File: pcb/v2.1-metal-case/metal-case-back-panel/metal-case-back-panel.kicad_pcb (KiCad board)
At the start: 2 copper layers, 50 x 20 mm, 6 parts

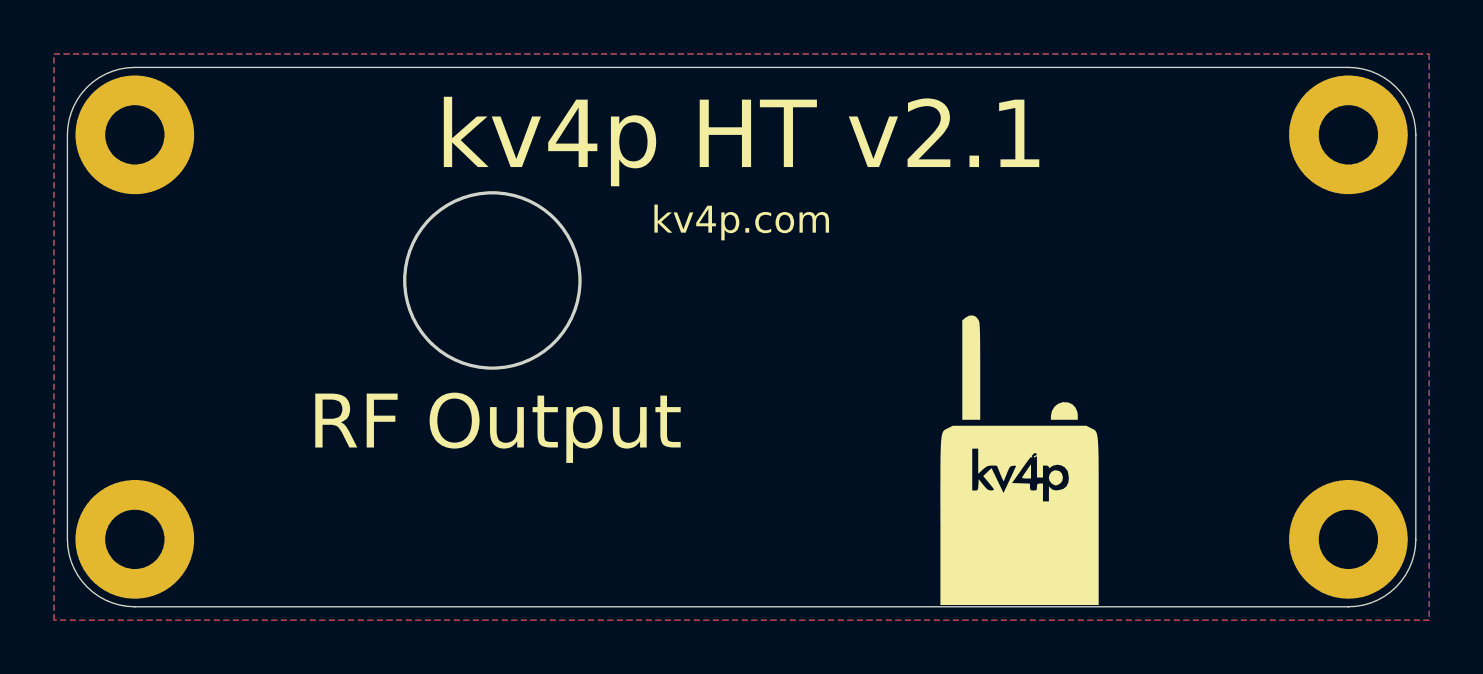
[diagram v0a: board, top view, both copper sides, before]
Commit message: v2.1b as ordered 2025-04-17. VHF and UHF #22. SAO headers. PTT buttons. User LED.
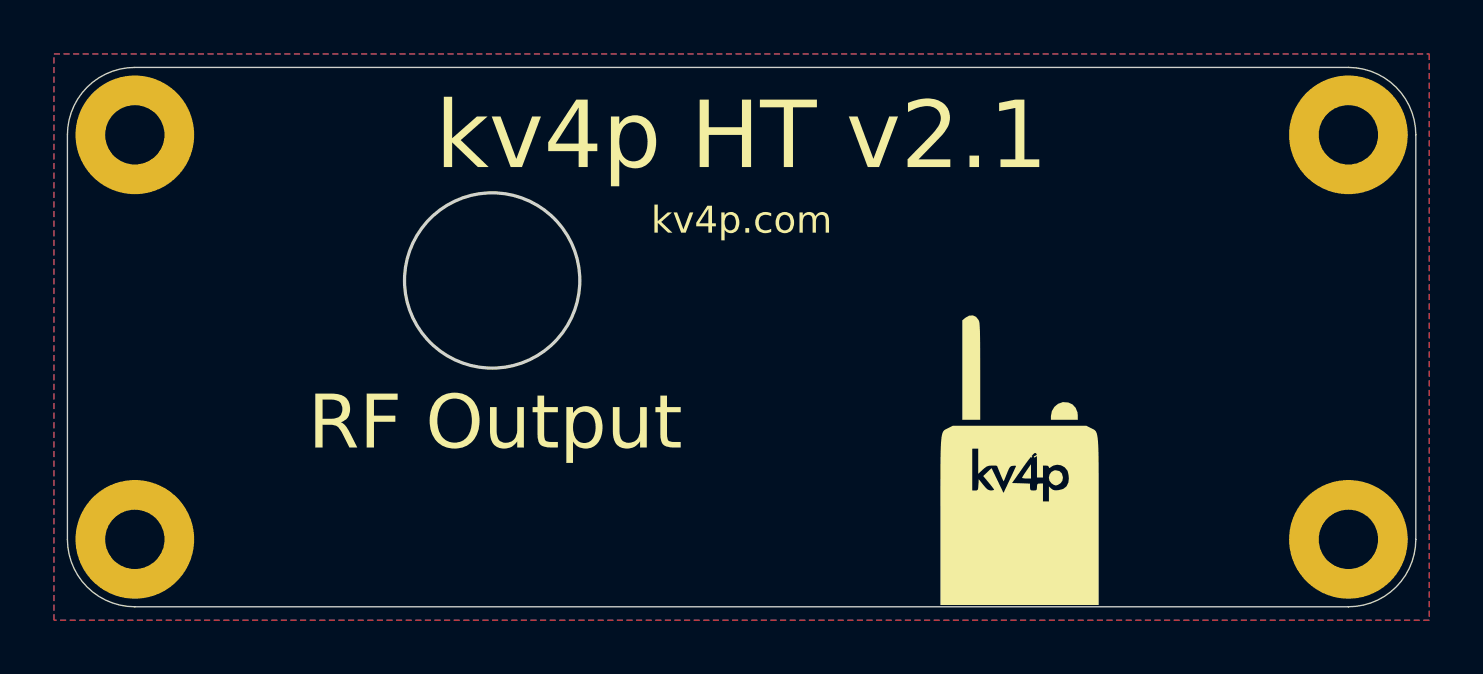
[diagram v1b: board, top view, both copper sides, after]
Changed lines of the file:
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@@
 	(footprint "Libraries:Conn_SMA_Panel_ThroughHole"
 		(layer "F.Cu")
-		(at 118.25732 110)
+		(at 118.25 110)
 		(property "Reference" "G2"
 			(at 0 -5.08 0)
@@
 		)
 	)
+	(dimension
+		(type aligned)
+		(layer "Dwgs.User")
+		(pts
+			(xy 127.5 110) (xy 118.25 110)
+		)
+		(height -8.75)
+		(gr_text "9.2500 mm"
+			(at 122.875 117.6 0)
+			(layer "Dwgs.User")
+			(effects
+				(font
+					(size 1 1)
+					(thickness 0.15)
+				)
+			)
+		)
+		(format
+			(prefix "")
+			(suffix "")
+			(units 3)
+			(units_format 1)
+			(precision 4)
+		)
+		(style
+			(thickness 0.1)
+			(arrow_length 1.27)
+			(text_position_mode 0)
+			(extension_height 0.58642)
+			(extension_offset 0.5) keep_text_aligned)
+	)
 	(zone
